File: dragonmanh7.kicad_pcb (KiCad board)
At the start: 4 copper layers, 135.6 x 54.6 mm, 119 parts, among them J1 USB_B, J10 Conn_02x12_Odd_Even, J11 Conn_02x03_Odd_Even, J12 VBAT+, J13 Conn_02x05_Odd_Even, J14 VBATG, J15 Conn_02x02_Odd_Even, J18 Conn_02x05_Odd_Even, J2 73725-0110BLF, J3 RJ45_Amphenol_RJMG1BD3B8K1ANR, J4 Micro_SD_Card, J5 Screw_Terminal_01x06, J6 Conn_02x12_Odd_Even, J7 USB_B, J8 Screw_Terminal_01x02, J9 Conn_02x12_Odd_Even, SW1 RESET, SW2 PC13, U1 STM32H743VITx, U10 USBLC6-2SC6, U12 TCAN332, U13 ISL83483, U14 MIC2005A, U2 KSZ8081RNA, U5 S25FL127SABMFI101, U6 AP63203, U7 USBLC6-2SC6, U8 STM32F042F6Px, U9 USBLC6-2SC6, Y1 8MHz, Y2 32.768KHz, Y3 25MHz

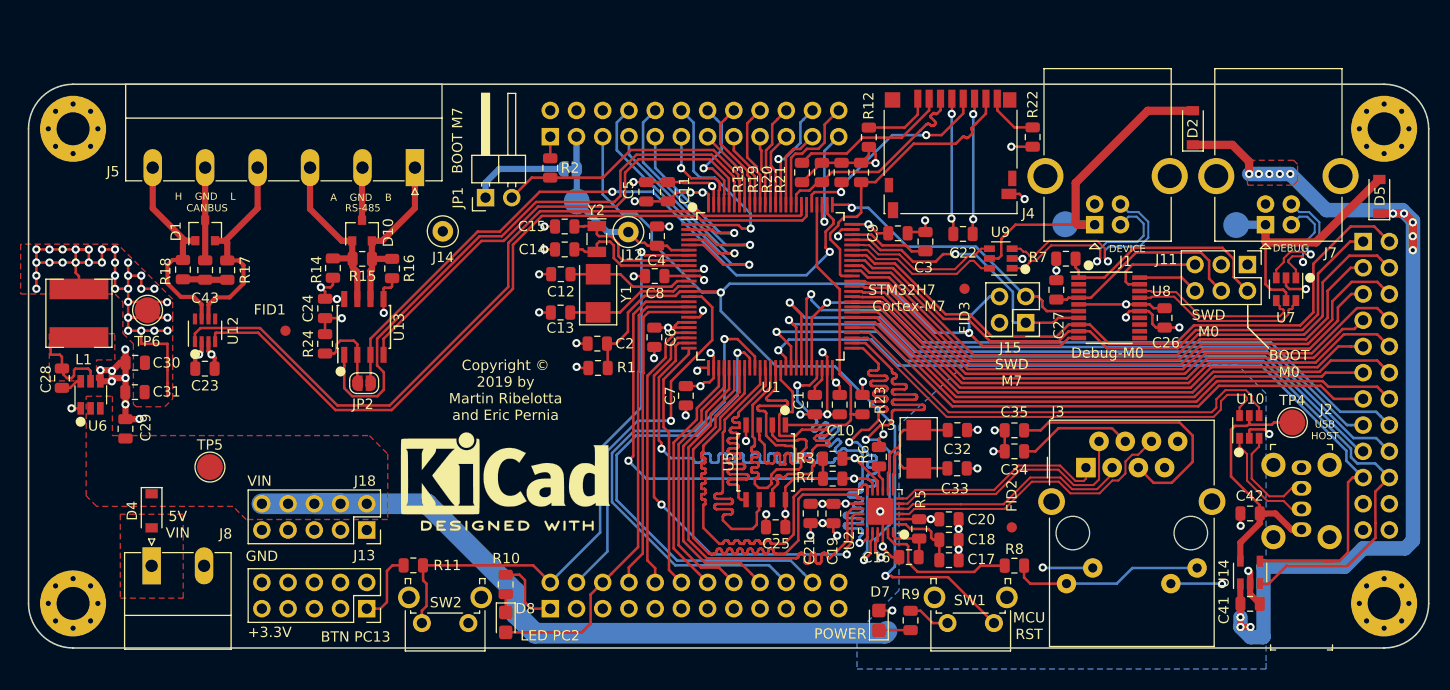
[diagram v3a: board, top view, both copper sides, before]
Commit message: Change PHY to LAN8742 and change power scheme to improve 5V handling
Signed-off-by: Martin Ribelotta <martinribelotta@gmail.com>
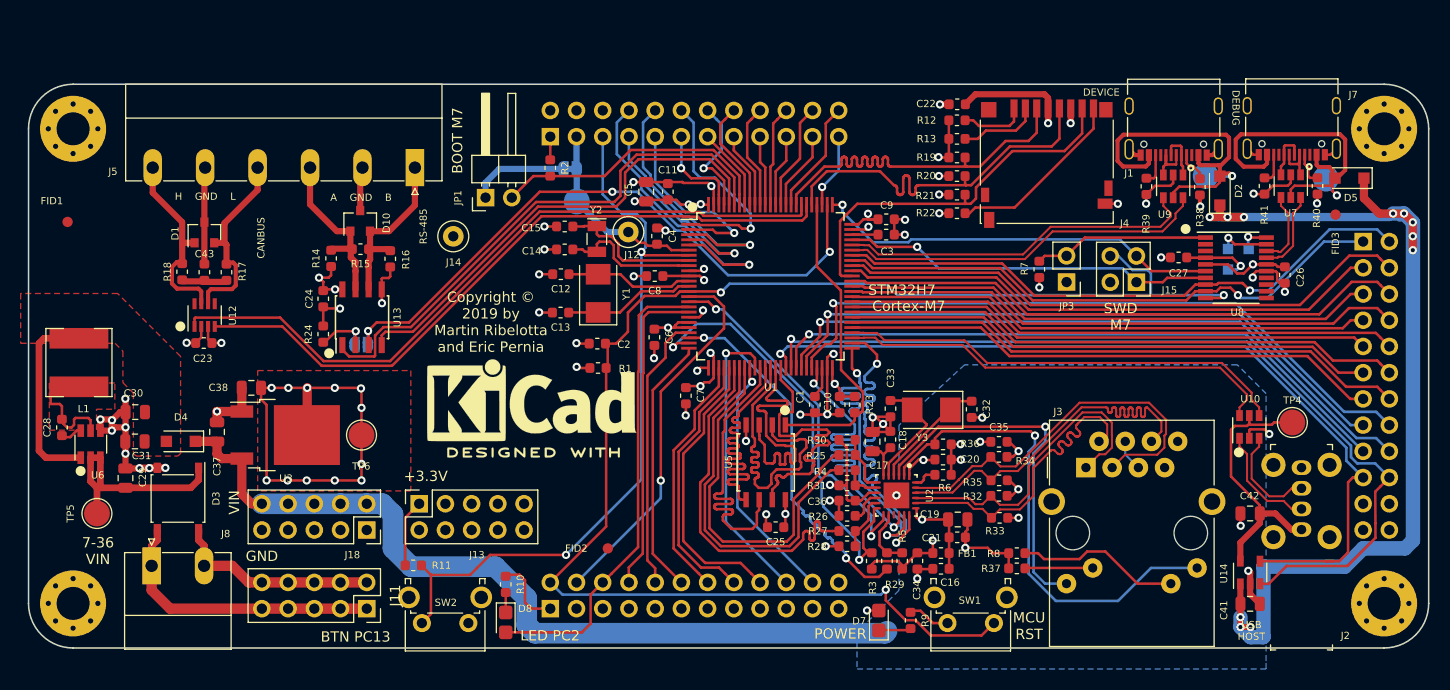
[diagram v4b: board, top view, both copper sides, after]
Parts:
- added C36: 0.1u, Capacitor_SMD:C_0603_1608Metric, F.Cu at (138.0, 68.3)
- added C37: 2.2u, Capacitor_SMD:C_0805_2012Metric, F.Cu at (76.9, 61.6)
- added C38: 2.2u, Capacitor_SMD:C_0805_2012Metric, F.Cu at (80.3, 57.4)
- added D3: ABS6UTR, Diode_SMD:Diode_Bridge_Diotec_ABS, F.Cu at (73.2, 68.1)
- added FB1: Ferrite_Bead, Inductor_SMD:L_0603_1608Metric, F.Cu at (147.1, 73.4)
- added JP3: BOOTB, Connector_PinHeader_2.54mm:PinHeader_1x02_P2.54mm_Vertical, F.Cu at (159.2, 47.1)
- added R25: 33R, Resistor_SMD:R_0603_1608Metric, F.Cu at (138.0, 63.9)
- added R26: 10K, Resistor_SMD:R_0603_1608Metric, F.Cu at (138.0, 69.7)
- added R27: 33R, Resistor_SMD:R_0603_1608Metric, F.Cu at (138.0, 71.2)
- added R28: 10K, Resistor_SMD:R_0603_1608Metric, F.Cu at (138.0, 72.7)
- added R29: 33R, Resistor_SMD:R_0603_1608Metric, F.Cu at (141.8, 74.1)
- added R30: 10K, Resistor_SMD:R_0603_1608Metric, F.Cu at (138.0, 62.4)
- added R31: 10K, Resistor_SMD:R_0603_1608Metric, F.Cu at (138.0, 66.8)
- added R32: 49.9R, Resistor_SMD:R_0603_1608Metric, F.Cu at (152.7, 67.8)
- added R33: 49.9R, Resistor_SMD:R_0603_1608Metric, F.Cu at (152.7, 69.9)
- added R34: 49.9R, Resistor_SMD:R_0603_1608Metric, F.Cu at (152.7, 64.0)
- added R35: 49.9R, Resistor_SMD:R_0603_1608Metric, F.Cu at (152.7, 66.3)
- added R36: 10K, Resistor_SMD:R_0603_1608Metric, F.Cu at (147.3, 62.8)
- added R37: 220R, Resistor_SMD:R_0603_1608Metric, F.Cu at (154.4, 74.8)
- added R38: 5K1, Resistor_SMD:R_0603_1608Metric, F.Cu at (172.1, 37.9)
- added R39: 5K1, Resistor_SMD:R_0603_1608Metric, F.Cu at (167.0, 37.8)
- added R40: 5K1, Resistor_SMD:R_0603_1608Metric, F.Cu at (183.5, 37.8)
- added R41: 5K1, Resistor_SMD:R_0603_1608Metric, F.Cu at (178.4, 37.8)
- added TP7: M0-SWDIO, TestPoint:TestPoint_Pad_1.0x1.0mm, B.Cu at (174.9, 43.9)
- added TP8: M0-SWCLK, TestPoint:TestPoint_Pad_1.0x1.0mm, B.Cu at (176.9, 43.9)
- added TP9: M0-RST, TestPoint:TestPoint_Pad_1.0x1.0mm, B.Cu at (174.9, 45.9)
- added U3: AZ1117CD-3.3TRG1, Package_TO_SOT_SMD:TO-252-2, F.Cu at (83.5, 61.9)
- C1, C10, C11, C12, C13, C14, C15, C16, C2, C20, C21, C22, C23, C24, C25, C26, C27, C28, C3, C34, C4, C43, C6, C7, C8, C9: footprint Capacitor_SMD:C_0805_2012Metric -> Capacitor_SMD:C_0603_1608Metric
- C18: value 4.7u -> 470p; footprint Capacitor_SMD:C_0805_2012Metric -> Capacitor_SMD:C_0603_1608Metric
- C19, C5: value 4.7u -> 10u
- C32, C33: value 22p -> 30p; footprint Capacitor_SMD:C_0805_2012Metric -> Capacitor_SMD:C_0603_1608Metric
- C35: value 0.1u -> 22n; footprint Capacitor_SMD:C_0805_2012Metric -> Capacitor_SMD:C_0603_1608Metric
- D2, D4, D5: value B120-E3 -> MBR120VLSFT3G; footprint Diode_SMD:D_SOD-123 -> Diode_SMD:D_SOD-123F
- J1, J7: value USB_B -> USB_C; footprint Connector_USB:USB_B_OST_USB-B1HSxx_Horizontal -> Connector_USB:USB_C_Receptacle_Palconn_UTC16-G
- J11: value Conn_02x03_Odd_Even -> Conn_02x05_Odd_Even; footprint Connector_PinHeader_2.54mm:PinHeader_2x03_P2.54mm_Vertical -> Connector_PinSocket_2.54mm:PinSocket_2x05_P2.54mm_Vertical
- JP2: moved to B.Cu
- L1: value 68uH -> 4.7u
- R1, R10, R11, R12, R13, R14, R15, R16, R17, R18, R19, R2, R20, R21, R22, R23, R24, R3, R7, R8, R9: footprint Resistor_SMD:R_0805_2012Metric -> Resistor_SMD:R_0603_1608Metric
- R4: value 4K7 -> 33R; footprint Resistor_SMD:R_0805_2012Metric -> Resistor_SMD:R_0603_1608Metric
- R5: value 4K7 -> 10K; footprint Resistor_SMD:R_0805_2012Metric -> Resistor_SMD:R_0603_1608Metric
- R6: value 6.49K 1% -> 12K1; footprint Resistor_SMD:R_0805_2012Metric -> Resistor_SMD:R_0603_1608Metric
- U2: value KSZ8081RNA -> LAN8742A-CZ-TR; footprint Package_DFN_QFN:QFN-24-1EP_4x4mm_P0.5mm_EP2.6x2.6mm -> footprints:Microchip-C04-143B-S4QFN-0-0-IPC_C
- U6: value AP63203 -> AP63205
- moved J11 91.6 mm to (91.4, 78.7)
- moved FID2 39.2 mm to (114.8, 72.9), turned to 90 degrees
- moved FID3 36.6 mm to (185.3, 40.6)
- moved TP6 24.0 mm to (90.9, 61.9)
- moved FID1 23.6 mm to (62.5, 41.3)
- moved U9 18.1 mm to (169.6, 37.8), turned to 270 degrees
- moved R13 15.4 mm to (148.6, 33.2), turned to 0 degrees
- moved C21 14.4 mm to (148.6, 71.8), turned to 180 degrees
- moved TP2 14.4 mm to (172.7, 36.8), turned to 270 degrees
- moved C34 14.2 mm to (144.8, 74.1), turned to 90 degrees
- moved C17 13.7 mm to (140.4, 62.6), turned to 90 degrees
- moved R19 13.2 mm to (148.6, 35.0), turned to 0 degrees
- moved U8 12.9 mm to (175.6, 45.7)
- moved C22 12.6 mm to (148.6, 29.9), turned to 180 degrees
- moved C26 12.4 mm to (180.4, 46.4)
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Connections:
- C16 pad 1: Net-(C16-Pad1) -> GND
- C16 pad 2: GND -> VDDETH
- C17 pad 1: Net-(C17-Pad1) -> 1V8ETH
- C18 pad 1: Net-(C17-Pad1) -> 1V8ETH
- C19 pad 1: +3V3 -> GND
- C19 pad 2: GND -> VDDETH
- C20 pad 1: +3V3 -> GND
- C20 pad 2: GND -> VDDETH
- C21 pad 1: +3V3 -> GND
- C21 pad 2: GND -> VDDETH
- C29 pad 1: VDC -> Net-(C29-Pad1)
- C30 pad 1: +3V3 -> VDC
- C31 pad 1: +3V3 -> VDC
- C34 pad 2: Net-(C34-Pad2) -> +3V3
- C35 pad 2: Net-(C35-Pad2) -> VDDETH
- C41 pad 1: VDC -> +5V
- D2 pad 1: VDC -> +5V
- D2 pad 2: /VBUS1 -> VBUS1
- D4 pad 1: VDC -> +5V
- D4 pad 2: Net-(D4-Pad2) -> VDC
- D5 pad 1: VDC -> +5V
- D5 pad 2: /VBUS2 -> VBUS2
- J10 pad 2: /PC13 -> /~RESET
- J11 pad 1: +3V3 -> VDINA
- J11 pad 2: /BOOT0_B -> VDINB
- J11 pad 3: GND -> VDINA
- J11 pad 4: /DBG_RST -> VDINB
- J11 pad 5: /SWDIO_B -> VDINA
- J11 pad 6: /SWCLK_B -> VDINB
- J18 pad 10: VDC -> +5V
- J18 pad 2: VDC -> +5V
- J18 pad 4: VDC -> +5V
- J18 pad 6: VDC -> +5V
- J18 pad 8: VDC -> +5V
- J3 pad L2: GND -> Net-(J3-PadL2)
- J3 pad L3: GND -> Net-(J3-PadL3)
- J3 pad L4: Net-(J3-PadL1) -> Net-(J3-PadL4)
- J3 pad R4: Net-(C34-Pad2) -> VDDETH
- J3 pad R5: Net-(C35-Pad2) -> VDDETH
- J3 pad R7: Net-(J3-PadR7) -> (no net)
- J8 pad 1: Net-(D4-Pad2) -> VDINA
- J8 pad 2: GND -> VDINB
- J9 pad 5: /~RESET -> /PC13
- L1 pad 2: +3V3 -> VDC
- R4 pad 1: /ENET_MDC -> /ENET_RXD0
- R4 pad 2: +3V3 -> /PHY_RXD0
- R5 pad 1: Net-(C16-Pad1) -> Net-(R29-Pad2)
- R8 pad 1: Net-(J3-PadL1) -> GND
- R8 pad 2: /ETH_LED -> Net-(J3-PadL2)
- TP2 pad 1: /VBUS1 -> VBUS1
- TP3 pad 1: /VBUS2 -> VBUS2
- TP5 pad 1: VDC -> Net-(C29-Pad1)
- U12 pad 5: Net-(U12-Pad5) -> (no net)
- U12 pad 8: Net-(U12-Pad8) -> (no net)
- U14 pad 1: VDC -> +5V
- U2 pad 1: Net-(C17-Pad1) -> VDDETH
- U2 pad 10: /ENET_MDIO -> Net-(R26-Pad2)
- U2 pad 11: /ENET_MDC -> /PHY_CRS_DV
- U2 pad 12: /ENET_RXD1 -> /ENET_MDIO
- U2 pad 13: /ENET_RXD0 -> /ENET_MDC
- U2 pad 14: +3V3 -> Net-(R29-Pad2)
- U2 pad 15: /ENET_CRS_DV -> (no net)
- U2 pad 16: /ENET_REF_CLK -> /ENET_TXEN
- U2 pad 17: Net-(U2-Pad17) -> /ENET_TXD0
- U2 pad 18: Net-(U2-Pad18) -> /ENET_TXD1
- U2 pad 19: /ENET_TXEN -> VDDETH
- U2 pad 2: +3V3 -> Net-(J3-PadL1)
- U2 pad 20: /ENET_TXD0 -> /TD-
- U2 pad 21: /ENET_TXD1 -> /TD+
- U2 pad 22: GND -> /RD-
- U2 pad 23: /ETH_LED -> /RD+
- U2 pad 24: Net-(C16-Pad1) -> Net-(R6-Pad1)
- U2 pad 3: /RD- -> Net-(J3-PadL4)
- U2 pad 4: /RD+ -> Net-(C32-Pad1)
- U2 pad 5: /TD- -> Net-(C33-Pad1)
- U2 pad 6: /TD+ -> 1V8ETH
- U2 pad 7: Net-(C33-Pad1) -> /PHY_RXD1
- U2 pad 8: Net-(C32-Pad1) -> /PHY_RXD0
- U2 pad 9: Net-(R6-Pad1) -> +3V3
- U6 pad 1: +3V3 -> VDC
- U6 pad 2: VDC -> Net-(C29-Pad1)
- U6 pad 3: VDC -> Net-(C29-Pad1)
- U7 pad 5: /VBUS2 -> VBUS2
- U8 pad 11: Net-(U8-Pad11) -> (no net)
- U8 pad 12: Net-(U8-Pad12) -> (no net)
- U8 pad 13: Net-(U8-Pad13) -> (no net)
- U8 pad 14: Net-(U8-Pad14) -> (no net)
- U8 pad 2: Net-(U8-Pad2) -> (no net)
- U8 pad 3: Net-(U8-Pad3) -> (no net)
- U9 pad 5: /VBUS1 -> VBUS1
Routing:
- net +5V: track 0.00 -> 183.1 mm, vias 0 -> 11
- net VDC: track 163.0 -> 18.8 mm, vias 13 -> 0
- net VDDETH: track 0.00 -> 56.7 mm, vias 0 -> 5
- net /VBUS1: track 35.4 -> 0.00 mm
- net Net-(J3-PadL4): track 0.00 -> 34.9 mm, vias 0 -> 1
- net VBUS2: track 0.00 -> 34.7 mm, vias 0 -> 1
- net VBUS1: track 0.00 -> 34.3 mm, vias 0 -> 1
- net Net-(J3-PadL1): track 18.8 -> 47.8 mm, vias 0 -> 1
- net VDINA: track 0.00 -> 27.7 mm
- net /VBUS2: track 27.0 -> 0.00 mm
- net Net-(C35-Pad2): track 26.4 -> 0.00 mm
- net GND: track 169.8 -> 194.0 mm, vias 56 -> 59
- net +3V3: track 173.5 -> 150.1 mm, vias 57 -> 36
- net /PB0: track 47.2 -> 24.5 mm
- net Net-(C29-Pad1): track 0.00 -> 20.9 mm
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- added copper zone on B.Cu, net +5V
- removed copper zone on F.Cu, net Net-(D4-Pad2)
- removed copper zone on B.Cu, net VDC
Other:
- board text added: "7-36 VIN"
- board text removed: "5V VIN"
- board text removed: "BOOT M0"
- board text removed: "Debug-M0"
- board text removed: "SWD M0"

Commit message: Improve schematic and PCB
Signed-off-by: Martin Ribelotta <martinribelotta@gmail.com>
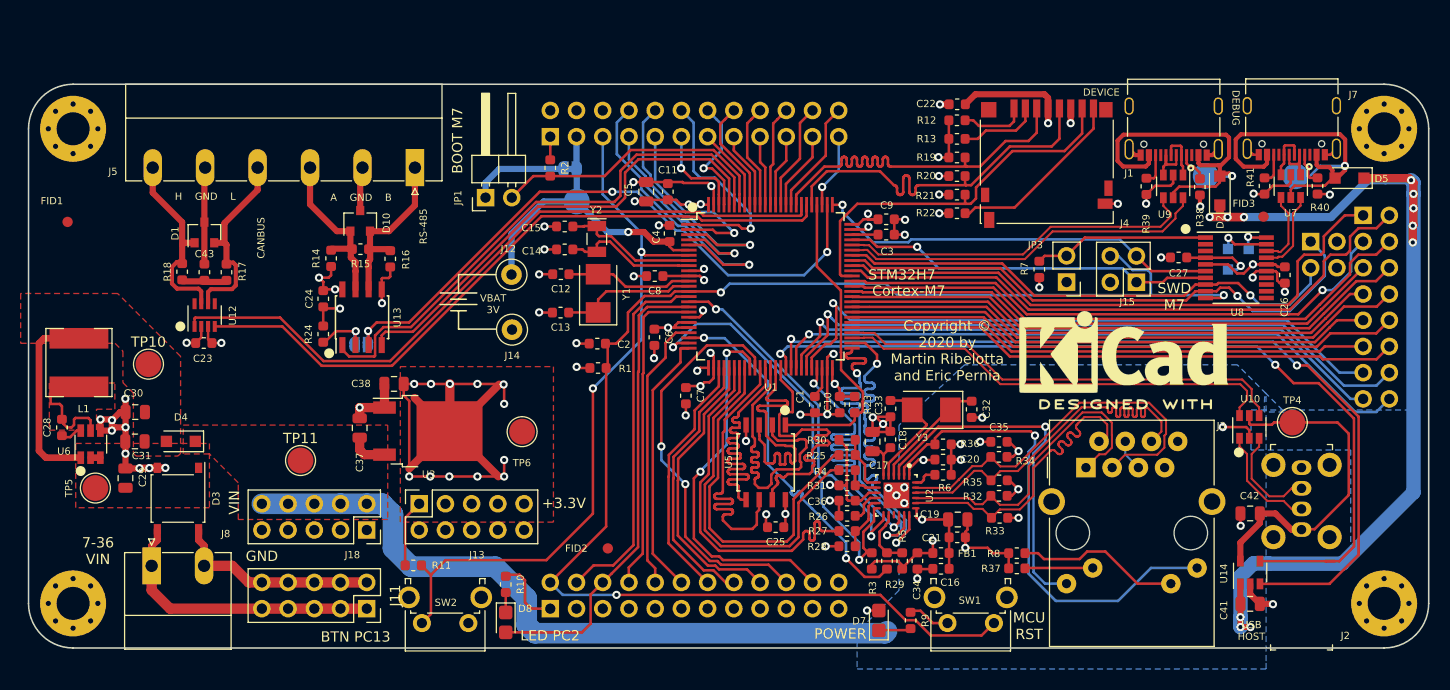
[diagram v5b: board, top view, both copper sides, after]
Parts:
- added J16: Conn_02x02_Odd_Even, Connector_PinSocket_2.54mm:PinSocket_2x02_P2.54mm_Vertical, B.Cu at (182.9, 43.2)
- added TP10: VDC_TP, TestPoint:TestPoint_Pad_D2.5mm, F.Cu at (70.3, 55.1)
- added TP11: 5V_TP, TestPoint:TestPoint_Pad_D2.5mm, F.Cu at (85.0, 64.4)
- J6: footprint Connector_PinSocket_2.54mm:PinSocket_2x12_P2.54mm_Vertical -> Connector_PinSocket_2.54mm:PinSocket_2x08_P2.54mm_Vertical
- moved LOGO1 57.5 mm to (164.8, 53.8)
- moved TP6 15.6 mm to (106.5, 61.6)
- moved C37 13.8 mm to (90.8, 61.2)
- moved C38 13.8 mm to (94.1, 57.0)
- moved U3 13.8 mm to (97.4, 61.5)
- moved J12 12.0 mm to (105.5, 46.4)
- moved J14 10.7 mm to (105.5, 51.7)
- moved FID3 6.98 mm to (178.3, 40.8), turned to 180 degrees
- moved TP3 2.96 mm to (181.4, 36.9)
- moved J6 2.54 mm to (188.0, 40.6)
- moved TP5 2.47 mm to (65.2, 67.1)
- moved C4 1.25 mm to (120.8, 42.4)
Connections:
- J6 pad 1: /U1_TX -> /PA8
- J6 pad 10: /PD13 -> /PD10
- J6 pad 11: /PD10 -> /PD9
- J6 pad 12: /PD11 -> /PD8
- J6 pad 13: /PD8 -> /PB10
- J6 pad 14: /PD9 -> /PE15
- J6 pad 15: /PE15 -> /PE14
- J6 pad 16: /PB10 -> /PE13
- J6 pad 2: /U1_RX -> /PC9
- J6 pad 3: /PC9 -> /PC7
- J6 pad 4: /PA8 -> /PC6
- J6 pad 5: /PC6 -> /PD15
- J6 pad 6: /PC7 -> /PD14
- J6 pad 7: /PD14 -> /PD13
- J6 pad 8: /PD15 -> /PD12
- J6 pad 9: /PD12 -> /PD11
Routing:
- net Net-(C29-Pad1): track 20.9 -> 0.95 mm
- net +3V3: track 150.1 -> 168.5 mm
- net +BATT: track 19.1 -> 31.0 mm, vias 0 -> 1
- net /PB0: track 24.5 -> 36.0 mm, vias 1 -> 2
- net /PB1: track 28.6 -> 39.1 mm, vias 1 -> 2
- net +5V: track 183.1 -> 173.1 mm
- net /U1_RX: track 57.4 -> 49.8 mm
- net /VBUS3: track 26.5 -> 33.0 mm
- net /PC9: track 52.8 -> 59.0 mm
- net /PC6: track 51.8 -> 57.1 mm
- net /PE14: track 65.5 -> 60.9 mm
- net /PD14: track 51.1 -> 55.7 mm
- net /PB10: track 66.4 -> 61.8 mm
- net /PD9: track 55.1 -> 50.9 mm
- net /PD12: track 51.1 -> 55.0 mm
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- added copper zone on F.Cu, net +5V
- added copper zone on F.Cu, net Net-(C29-Pad1)
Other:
- board text added: "Copyright © 2020 by Martin Ribelotta and Eric Pernia"
- board text added: "VBAT 3V"
- board text removed: "Copyright © 2019 by Martin Ribelotta and Eric Pernia"

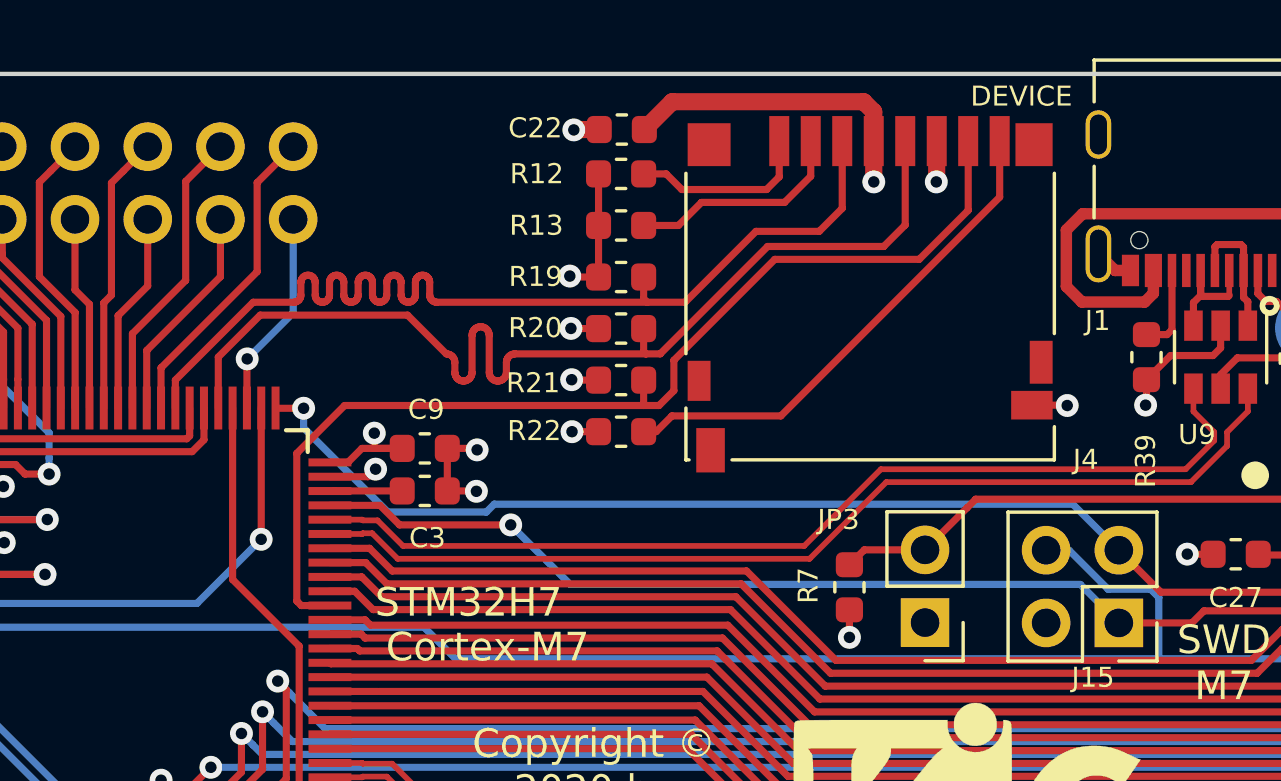
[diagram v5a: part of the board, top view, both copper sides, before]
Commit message: Change uSD card connector by Molex 1051620001
Signed-off-by: Martin Ribelotta <martinribelotta@gmail.com>
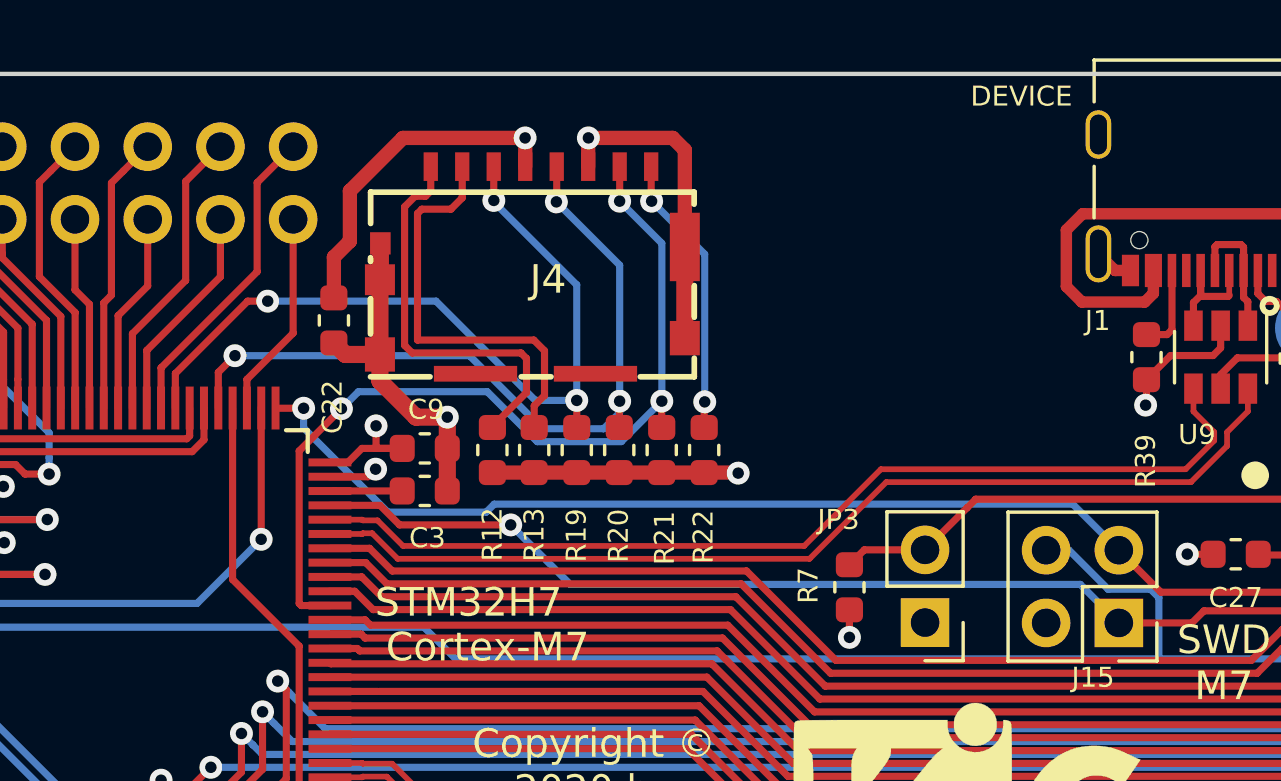
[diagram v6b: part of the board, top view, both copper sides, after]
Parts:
- J4: value Micro_SD_Card -> 105162-0001; footprint Connector_Card:microSD_HC_Hirose_DM3D-SF -> footprints:105162-0001
- moved J4 12.1 mm to (145.5, 38.5)
- moved C22 12.1 mm to (138.6, 36.6), turned to 270 degrees
- moved R12 10.6 mm to (144.1, 41.1), turned to 90 degrees
- moved R13 8.41 mm to (145.6, 41.1), turned to 90 degrees
- moved R19 6.24 mm to (147.1, 41.1), turned to 90 degrees
- moved R20 4.24 mm to (148.6, 41.1), turned to 90 degrees
- moved R22 2.97 mm to (151.5, 41.1), turned to 90 degrees
- moved R21 2.82 mm to (150.0, 41.1), turned to 90 degrees
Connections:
- J4 pad 10: (no net) -> GND
- J4 pad 11: (no net) -> GND
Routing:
- net GND: track 194.9 -> 210.9 mm, vias 62 -> 59
- net /SDMMC_CLK: track 37.3 -> 27.2 mm, vias 0 -> 3
- net /SDMMC_CMD: track 37.3 -> 28.0 mm, vias 0 -> 3
- net /SDMMC_D1: track 17.8 -> 9.89 mm, vias 0 -> 2
- net /SDMMC_D2: track 6.40 -> 14.2 mm
- net /SDMMC_D3: track 7.78 -> 14.7 mm
- net /SDMMC_D0: track 37.3 -> 31.0 mm, vias 0 -> 3
- net +3V3: track 168.5 -> 170.6 mm, vias 36 -> 33
- net /PC10: vias 1 -> 0
